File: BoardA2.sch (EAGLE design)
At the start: 4 parts, among them J1 CONN_12X2

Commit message: Update
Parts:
- removed J1: CONN_12X2, Smartcrutches:CONN_12X2
- added OSC: CLOCK-ECS-100X, Smartcrutches:CLOCK-ECS-100X
- C1: value (none) -> 0.1 uf
- IMU: value (none) -> AD7890-10
- U$1: value CLOCK-ECS-100X -> LOADCELLAMP; device Smartcrutches:CLOCK-ECS-100X -> Smartcrutches:LOADCELLAMP
- renumbered IC1 to IMU
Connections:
- new net CONVST: IMU.5
- new net DIN: IMU.11
- new net DOUT: IMU.10
- new net N$10: U$1.E+
- new net N$11: IMU.4
- new net N$12: U$1.E-
- new net N$13: U$1.A-
- new net N$14: U$1.A+
- new net N$15: U$1.SD
- new net N$7: U$1.DAT
- new net N$8: U$1.CLK
- new net RFS: IMU.9
- new net SCLK: IMU.7
- new net TFS: IMU.8
- new net UPPER1: IMU.16
- net 5V: now also OSC.+5V, U$1.VCC, U$1.VDD; no longer U$1.+5V
- net GND: now also C1.2, IMU.24, OSC.GND
- net N$2: now also IMU.17; no longer C1.2, IMU.24
- net N$4: now also OSC.OUT; no longer U$1.OUT

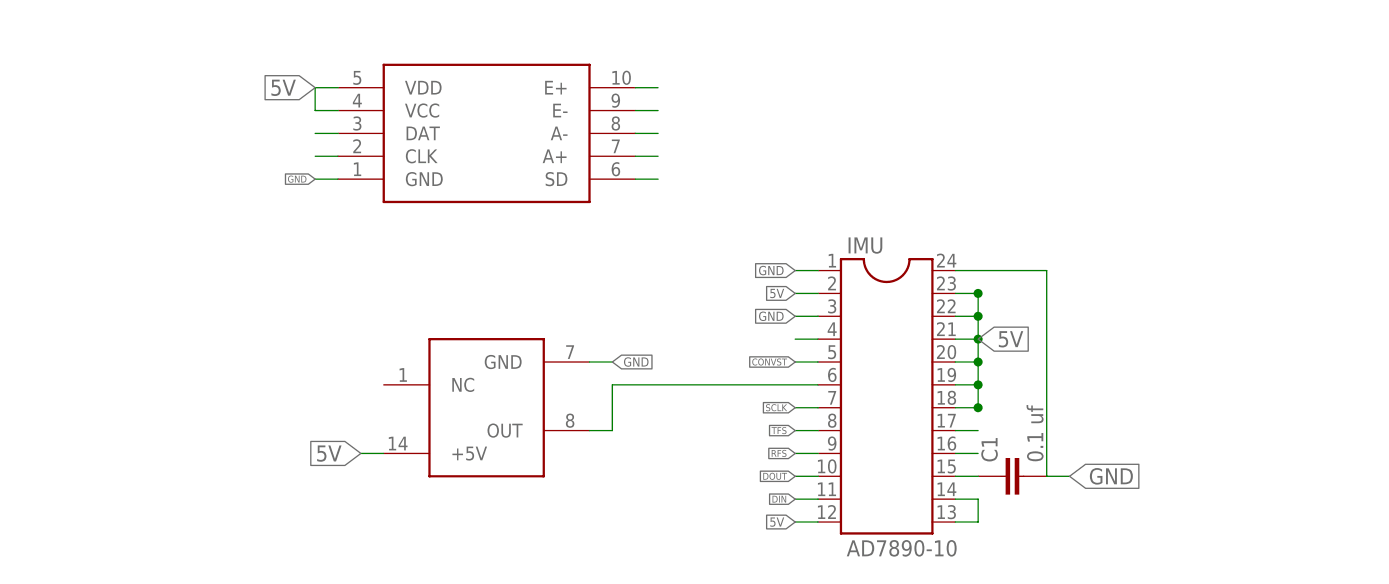
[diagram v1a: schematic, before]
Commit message: Updated both Boards
- Added holes
- Changed connectors
- routed both Boards
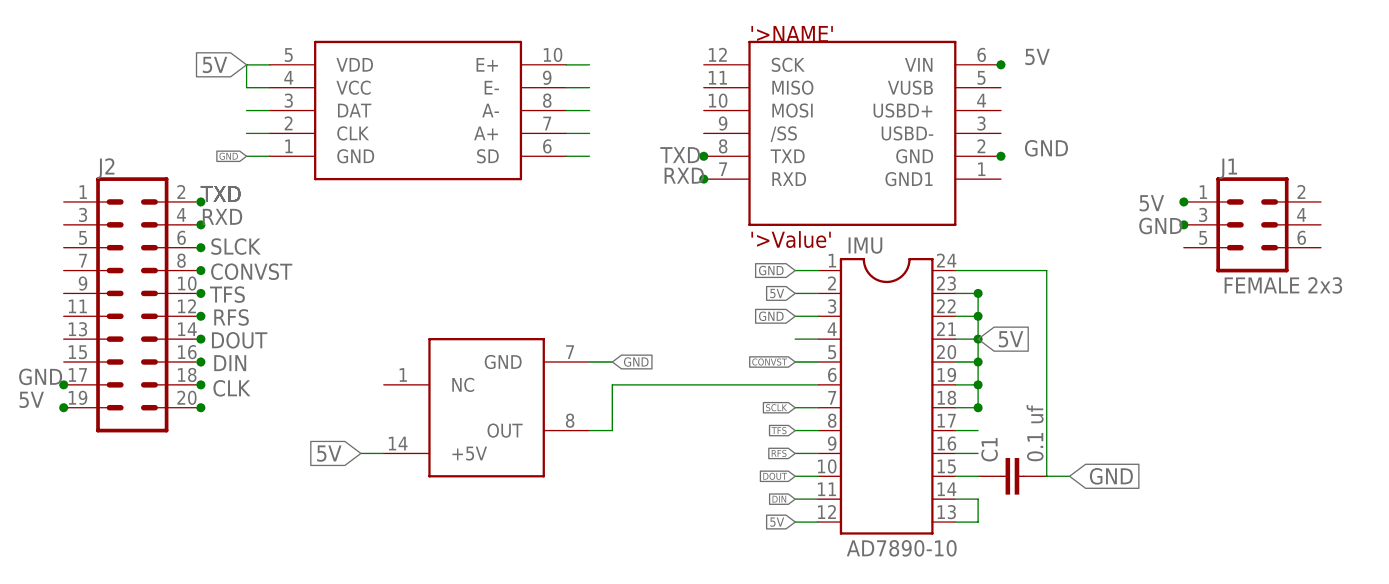
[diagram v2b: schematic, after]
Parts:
- added J1: FEMALE 2x3, SparkFun-Connectors:CONN_03X2FEMALE
- added J2: (no value), SparkFun-Connectors:CONN_10X2
- added U$2: IMU, Smartcrutches:IMU
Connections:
- new net CLK: J2.18
- new net N$22: J2.20
- new net RXD: J2.4, U$2.RXD
- new net SLCK: J2.6
- new net TXD: J2.2, U$2.TXD
- net 5V: now also IMU.2, J1.1, J2.19, U$2.VIN
- net CONVST: now also J2.8
- net DIN: now also J2.16
- net DOUT: now also J2.14
- net GND: now also IMU.1, J1.3, J2.17, U$2.GND
- net RFS: now also J2.12
- net TFS: now also J2.10
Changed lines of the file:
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@@
 <layer number="49" name="Reference" color="7" fill="1" visible="no" active="no"/>
 <layer number="50" name="dxf" color="7" fill="1" visible="no" active="no"/>
-<layer number="51" name="tDocu" color="9" fill="1" visible="no" active="no"/>
+<layer number="51" name="tDocu" color="7" fill="1" visible="no" active="no"/>
 <layer number="52" name="bDocu" color="7" fill="1" visible="no" active="no"/>
 <layer number="53" name="tGND_GNDA" color="7" fill="9" visible="no" active="no"/>
@@
 <part name="C1" library="SparkFun-Capacitors" deviceset="0.1UF-50V-20%(PTH)" device="KIT-EZ" value="0.1 uf"/>
 <part name="U$1" library="Smartcrutches" deviceset="LOADCELLAMP" device=""/>
+<part name="J1" library="SparkFun-Connectors" deviceset="CONN_03X2" device="FEMALE" value="FEMALE 2x3"/>
+<part name="U$2" library="Smartcrutches" deviceset="IMU" device=""/>
+<part name="J2" library="SparkFun-Connectors" deviceset="CONN_10X2" device=""/>
 </parts>
 <sheets>
@@
 <instance part="IMU" gate="G$1" x="-5.08" y="48.26"/>
 <instance part="C1" gate="G$1" x="10.16" y="40.64" rot="R90"/>
-<instance part="U$1" gate="G$1" x="-48.26" y="78.74"/>
+<instance part="U$1" gate="G$1" x="-55.88" y="81.28"/>
+<instance part="J1" gate="G$1" x="35.56" y="68.58"/>
+<instance part="U$2" gate="G$1" x="-10.16" y="78.74"/>
+<instance part="J2" gate="G$1" x="-88.9" y="60.96"/>
 </instances>
 <busses>
@@
 <segment>
 <wire x1="-12.7" y1="60.96" x2="-15.24" y2="60.96" width="0.1524" layer="91"/>
+<pinref part="IMU" gate="G$1" pin="2"/>
 </segment>
 <segment>
 <pinref part="U$1" gate="G$1" pin="VCC"/>
-<wire x1="-66.04" y1="81.28" x2="-68.58" y2="81.28" width="0.1524" layer="91"/>
+<wire x1="-73.66" y1="83.82" x2="-76.2" y2="83.82" width="0.1524" layer="91"/>
 <pinref part="U$1" gate="G$1" pin="VDD"/>
-<wire x1="-66.04" y1="83.82" x2="-68.58" y2="83.82" width="0.1524" layer="91"/>
-<wire x1="-68.58" y1="81.28" x2="-68.58" y2="83.82" width="0.1524" layer="91"/>
-<label x="-68.58" y="83.82" size="1.778" layer="95" rot="R180" xref="yes"/>
+<wire x1="-73.66" y1="86.36" x2="-76.2" y2="86.36" width="0.1524" layer="91"/>
+<wire x1="-76.2" y1="83.82" x2="-76.2" y2="86.36" width="0.1524" layer="91"/>
+<label x="-76.2" y="86.36" size="1.778" layer="95" rot="R180" xref="yes"/>
+</segment>
+<segment>
+<pinref part="J1" gate="G$1" pin="1"/>
+<junction x="27.94" y="71.12"/>
+<label x="22.86" y="70.104" size="1.778" layer="95"/>
+</segment>
+<segment>
+<pinref part="U$2" gate="G$1" pin="VIN"/>
+<junction x="7.62" y="86.36"/>
+<label x="10.16" y="86.36" size="1.778" layer="95"/>
+</segment>
+<segment>
+<pinref part="J2" gate="G$1" pin="19"/>
+<junction x="-96.52" y="48.26"/>
+<label x="-101.6" y="48.26" size="1.778" layer="95"/>
 </segment>
 </net>
@@
 <wire x1="-12.7" y1="63.5" x2="-15.24" y2="63.5" width="0.1524" layer="91"/>
 <label x="-15.24" y="63.5" size="1.016" layer="95" rot="R180" xref="yes"/>
+<pinref part="IMU" gate="G$1" pin="1"/>
 </segment>
 <segment>
@@
 <segment>
 <pinref part="U$1" gate="G$1" pin="GND"/>
-<wire x1="-66.04" y1="73.66" x2="-68.58" y2="73.66" width="0.1524" layer="91"/>
-<label x="-68.58" y="73.66" size="0.762" layer="95" rot="R180" xref="yes"/>
+<wire x1="-73.66" y1="76.2" x2="-76.2" y2="76.2" width="0.1524" layer="91"/>
+<label x="-76.2" y="76.2" size="0.762" layer="95" rot="R180" xref="yes"/>
+</segment>
+<segment>
+<pinref part="J1" gate="G$1" pin="3"/>
+<junction x="27.94" y="68.58"/>
+<label x="22.86" y="67.564" size="1.778" layer="95"/>
+</segment>
+<segment>
+<pinref part="U$2" gate="G$1" pin="GND"/>
+<junction x="7.62" y="76.2"/>
+<label x="10.16" y="76.2" size="1.778" layer="95"/>
+</segment>
+<segment>
+<pinref part="J2" gate="G$1" pin="17"/>
+<junction x="-96.52" y="50.8"/>
+<label x="-101.6" y="50.8" size="1.778" layer="95"/>
 </segment>
 </net>
@@
 <label x="-15.24" y="38.1" size="0.762" layer="95" rot="R180" xref="yes"/>
 </segment>
+<segment>
+<pinref part="J2" gate="G$1" pin="16"/>
+<junction x="-81.28" y="53.34"/>
+<label x="-80.01" y="52.324" size="1.778" layer="95"/>
+</segment>
 </net>
 <net name="DOUT" class="0">
@@
 <label x="-15.24" y="40.64" size="0.762" layer="95" rot="R180" xref="yes"/>
 </segment>
+<segment>
+<pinref part="J2" gate="G$1" pin="14"/>
+<junction x="-81.28" y="55.88"/>
+<label x="-80.264" y="54.864" size="1.778" layer="95"/>
+</segment>
 </net>
 <net name="RFS" class="0">
@@
 <label x="-15.24" y="43.18" size="0.762" layer="95" rot="R180" xref="yes"/>
 </segment>
+<segment>
+<pinref part="J2" gate="G$1" pin="12"/>
+<junction x="-81.28" y="58.42"/>
+<label x="-80.01" y="57.404" size="1.778" layer="95"/>
+</segment>
 </net>
 <net name="TFS" class="0">
@@
 <label x="-15.24" y="45.72" size="0.762" layer="95" rot="R180" xref="yes"/>
 </segment>
+<segment>
+<pinref part="J2" gate="G$1" pin="10"/>
+<junction x="-81.28" y="60.96"/>
+<label x="-80.264" y="59.944" size="1.778" layer="95"/>
+</segment>
 </net>
 <net name="SCLK" class="0">
@@
 <label x="-15.24" y="53.34" size="0.762" layer="95" rot="R180" xref="yes"/>
 </segment>
+<segment>
+<pinref part="J2" gate="G$1" pin="8"/>
+<junction x="-81.28" y="63.5"/>
+<label x="-80.264" y="62.484" size="1.778" layer="95"/>
+</segment>
 </net>
 <net name="N$11" class="0">
@@
 <segment>
 <pinref part="U$1" gate="G$1" pin="DAT"/>
-<wire x1="-66.04" y1="78.74" x2="-68.58" y2="78.74" width="0.1524" layer="91"/>
+<wire x1="-73.66" y1="81.28" x2="-76.2" y2="81.28" width="0.1524" layer="91"/>
 </segment>
 </net>
@@
 <segment>
 <pinref part="U$1" gate="G$1" pin="CLK"/>
-<wire x1="-66.04" y1="76.2" x2="-68.58" y2="76.2" width="0.1524" layer="91"/>
+<wire x1="-73.66" y1="78.74" x2="-76.2" y2="78.74" width="0.1524" layer="91"/>
 </segment>
 </net>
@@
 <segment>
 <pinref part="U$1" gate="G$1" pin="E+"/>
-<wire x1="-33.02" y1="83.82" x2="-30.48" y2="83.82" width="0.1524" layer="91"/>
+<wire x1="-40.64" y1="86.36" x2="-38.1" y2="86.36" width="0.1524" layer="91"/>
 </segment>
 </net>
@@
 <segment>
 <pinref part="U$1" gate="G$1" pin="E-"/>
-<wire x1="-33.02" y1="81.28" x2="-30.48" y2="81.28" width="0.1524" layer="91"/>
+<wire x1="-40.64" y1="83.82" x2="-38.1" y2="83.82" width="0.1524" layer="91"/>
 </segment>
 </net>
@@
 <segment>
 <pinref part="U$1" gate="G$1" pin="A-"/>
-<wire x1="-33.02" y1="78.74" x2="-30.48" y2="78.74" width="0.1524" layer="91"/>
+<wire x1="-40.64" y1="81.28" x2="-38.1" y2="81.28" width="0.1524" layer="91"/>
 </segment>
 </net>
@@
 <segment>
 <pinref part="U$1" gate="G$1" pin="A+"/>
-<wire x1="-33.02" y1="76.2" x2="-30.48" y2="76.2" width="0.1524" layer="91"/>
+<wire x1="-40.64" y1="78.74" x2="-38.1" y2="78.74" width="0.1524" layer="91"/>
 </segment>
 </net>
@@
 <segment>
 <pinref part="U$1" gate="G$1" pin="SD"/>
-<wire x1="-33.02" y1="73.66" x2="-30.48" y2="73.66" width="0.1524" layer="91"/>
-</segment>
-</net>
+<wire x1="-40.64" y1="76.2" x2="-38.1" y2="76.2" width="0.1524" layer="91"/>
+</segment>
+</net>
+<net name="TXD" class="0">
+<segment>
+<pinref part="J2" gate="G$1" pin="2"/>
+<junction x="-81.28" y="71.12"/>
+<label x="-81.28" y="71.12" size="1.778" layer="95"/>
+<label x="-81.28" y="71.12" size="1.778" layer="95"/>
+<label x="-81.28" y="71.12" size="1.778" layer="95"/>
+</segment>
+<segment>
+<pinref part="U$2" gate="G$1" pin="TXD"/>
+<junction x="-25.4" y="76.2"/>
+<label x="-30.226" y="75.438" size="1.778" layer="95"/>
+</segment>
+</net>
+<net name="RXD" class="0">
+<segment>
+<pinref part="J2" gate="G$1" pin="4"/>
+<junction x="-81.28" y="68.58"/>
+<label x="-81.28" y="68.58" size="1.778" layer="95"/>
+</segment>
+<segment>
+<pinref part="U$2" gate="G$1" pin="RXD"/>
+<junction x="-25.4" y="73.66"/>
+<label x="-29.972" y="73.152" size="1.778" layer="95"/>
+</segment>
+</net>
+<net name="SLCK" class="0">
+<segment>
+<pinref part="J2" gate="G$1" pin="6"/>
+<junction x="-81.28" y="66.04"/>
+<label x="-80.264" y="65.278" size="1.778" layer="95"/>
+</segment>
+</net>
+<net name="CLK" class="0">
+<segment>
+<pinref part="J2" gate="G$1" pin="18"/>
+<junction x="-81.28" y="50.8"/>
+<label x="-80.01" y="49.53" size="1.778" layer="95"/>
+</segment>
+</net>
+<net name="N$22" class="0">
+<segment>
+<pinref part="J2" gate="G$1" pin="20"/>
+<junction x="-81.28" y="48.26"/>
+</segment>
+</net>

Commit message: Routing Update
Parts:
- removed U$1: LOADCELLAMP, Smartcrutches:LOADCELLAMP
- removed U$2: IMU, Smartcrutches:IMU
- added ADC: AD7890-10, ic-package:DIL24-4
- added LOADCELL_AMP: HX711, Smartcrutches:LOADCELLAMP
- IMU: value AD7890-10 -> TSS-EM/3Space; device ic-package:DIL24-4 -> Smartcrutches:IMU
- renumbered OSC to OSCILLATOR
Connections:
- removed net N$10: U$1.E+
- removed net N$12: U$1.E-
- removed net N$13: U$1.A-
- removed net N$14: U$1.A+
- removed net N$15: U$1.SD
- removed net N$7: U$1.DAT
- removed net N$8: U$1.CLK
- net 5V: now also ADC.12, ADC.18, ADC.19, ADC.2, ADC.20, ADC.21, ADC.22, ADC.23, IMU.VIN, LOADCELL_AMP.VCC, LOADCELL_AMP.VDD; no longer IMU.12, IMU.18, IMU.19, IMU.2, IMU.20, IMU.21, IMU.22, IMU.23, U$1.VCC, U$1.VDD, U$2.VIN
- net CONVST: now also ADC.5; no longer IMU.5
- net DIN: now also ADC.11; no longer IMU.11
- net DOUT: now also ADC.10; no longer IMU.10
- net GND: now also ADC.1, ADC.24, ADC.3, IMU.GND, LOADCELL_AMP.GND; no longer IMU.1, IMU.24, IMU.3, U$1.GND, U$2.GND
- net N$1: now also ADC.13, ADC.14; no longer IMU.13, IMU.14
- net N$11: now also ADC.4; no longer IMU.4
- net N$2: now also ADC.17; no longer IMU.17
- net N$3: now also ADC.15; no longer IMU.15
- net N$4: now also ADC.6; no longer IMU.6
- net RFS: now also ADC.9; no longer IMU.9
- net RXD: now also IMU.RXD; no longer U$2.RXD
- net SCLK: now also ADC.7; no longer IMU.7
- net TFS: now also ADC.8; no longer IMU.8
- net TXD: now also IMU.TXD; no longer U$2.TXD
- net UPPER1: now also ADC.16; no longer IMU.16

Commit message: Routing and connection update
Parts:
- added J3: (no value), SparkFun-Connectors:CONN_04
- added J4: (no value), SparkFun-Connectors:CONN_01
- J2: device SparkFun-Connectors:CONN_10X2 -> SparkFun-Connectors:CONN_04
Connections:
- removed net CLK: J2.18
- removed net N$22: J2.20
- net 5V: no longer J2.19
- net CONVST: now also J4.1; no longer J2.8
- net DIN: now also J2.4; no longer J2.16
- net DOUT: now also J2.3; no longer J2.14
- net GND: no longer J2.17
- net RFS: now also J3.4; no longer J2.12
- net RXD: now also J2.2; no longer J2.4
- net SLCK: now also J3.1; no longer J2.6
- net TFS: now also J3.3; no longer J2.10
- net TXD: now also J2.1; no longer J2.2
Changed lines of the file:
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@@
 <part name="J1" library="SparkFun-Connectors" deviceset="CONN_03X2" device="FEMALE" value="FEMALE 2x3"/>
 <part name="IMU" library="Smartcrutches" deviceset="IMU" device="" value="TSS-EM/3Space"/>
-<part name="J2" library="SparkFun-Connectors" deviceset="CONN_10X2" device=""/>
 <part name="LOADCELL_AMP" library="Smartcrutches" deviceset="LOADCELLAMP" device="" value="HX711"/>
+<part name="J2" library="SparkFun-Connectors" deviceset="CONN_04" device=""/>
+<part name="J3" library="SparkFun-Connectors" deviceset="CONN_04" device=""/>
+<part name="J4" library="SparkFun-Connectors" deviceset="CONN_01" device=""/>
 </parts>
 <sheets>
@@
 <instance part="J1" gate="G$1" x="35.56" y="68.58"/>
 <instance part="IMU" gate="G$1" x="-7.62" y="83.82"/>
-<instance part="J2" gate="G$1" x="-88.9" y="60.96"/>
 <instance part="LOADCELL_AMP" gate="G$1" x="-55.88" y="86.36"/>
+<instance part="J2" gate="G$1" x="-35.56" y="68.58"/>
+<instance part="J3" gate="G$1" x="25.4" y="86.36"/>
+<instance part="J4" gate="G$1" x="-60.96" y="71.12"/>
 </instances>
 <busses>
@@
 </segment>
 <segment>
-<pinref part="J2" gate="G$1" pin="19"/>
-<junction x="-96.52" y="48.26"/>
-<label x="-101.6" y="48.26" size="1.778" layer="95"/>
-</segment>
-<segment>
 <pinref part="LOADCELL_AMP" gate="G$1" pin="VDD"/>
 <junction x="-73.66" y="91.44"/>
@@
 </segment>
 <segment>
-<pinref part="J2" gate="G$1" pin="17"/>
-<junction x="-96.52" y="50.8"/>
-<label x="-101.6" y="50.8" size="1.778" layer="95"/>
-</segment>
-<segment>
 <pinref part="LOADCELL_AMP" gate="G$1" pin="GND"/>
 <junction x="-73.66" y="81.28"/>
@@
 </segment>
 <segment>
-<pinref part="J2" gate="G$1" pin="16"/>
-<junction x="-81.28" y="53.34"/>
-<label x="-80.01" y="52.324" size="1.778" layer="95"/>
+<pinref part="J2" gate="G$1" pin="4"/>
+<junction x="-30.48" y="73.66"/>
+<label x="-29.718" y="72.898" size="1.778" layer="95"/>
 </segment>
 </net>
@@
 </segment>
 <segment>
-<pinref part="J2" gate="G$1" pin="14"/>
-<junction x="-81.28" y="55.88"/>
-<label x="-80.264" y="54.864" size="1.778" layer="95"/>
+<pinref part="J2" gate="G$1" pin="3"/>
+<junction x="-30.48" y="71.12"/>
+<label x="-29.972" y="70.358" size="1.778" layer="95"/>
 </segment>
 </net>
@@
 </segment>
 <segment>
-<pinref part="J2" gate="G$1" pin="12"/>
-<junction x="-81.28" y="58.42"/>
-<label x="-80.01" y="57.404" size="1.778" layer="95"/>
+<pinref part="J3" gate="G$1" pin="4"/>
+<junction x="30.48" y="91.44"/>
+<label x="30.988" y="90.678" size="1.778" layer="95"/>
 </segment>
 </net>
@@
 </segment>
 <segment>
-<pinref part="J2" gate="G$1" pin="10"/>
-<junction x="-81.28" y="60.96"/>
-<label x="-80.264" y="59.944" size="1.778" layer="95"/>
+<pinref part="J3" gate="G$1" pin="3"/>
+<junction x="30.48" y="88.9"/>
+<label x="31.242" y="87.884" size="1.778" layer="95"/>
 </segment>
 </net>
@@
 </segment>
 <segment>
-<pinref part="J2" gate="G$1" pin="8"/>
-<junction x="-81.28" y="63.5"/>
-<label x="-80.264" y="62.484" size="1.778" layer="95"/>
+<pinref part="J4" gate="G$1" pin="1"/>
+<junction x="-53.34" y="71.12"/>
+<label x="-52.324" y="70.358" size="1.778" layer="95"/>
 </segment>
 </net>
@@
 </net>
 <net name="TXD" class="0">
-<segment>
-<pinref part="J2" gate="G$1" pin="2"/>
-<junction x="-81.28" y="71.12"/>
-<label x="-81.28" y="71.12" size="1.778" layer="95"/>
-<label x="-81.28" y="71.12" size="1.778" layer="95"/>
-<label x="-81.28" y="71.12" size="1.778" layer="95"/>
-</segment>
 <segment>
 <pinref part="IMU" gate="G$1" pin="TXD"/>
@@
 <label x="-22.86" y="81.28" size="1.016" layer="95" rot="R180" xref="yes"/>
 </segment>
+<segment>
+<pinref part="J2" gate="G$1" pin="1"/>
+<junction x="-30.48" y="66.04"/>
+<label x="-29.972" y="65.278" size="1.778" layer="95"/>
+</segment>
 </net>
 <net name="RXD" class="0">
-<segment>
-<pinref part="J2" gate="G$1" pin="4"/>
-<junction x="-81.28" y="68.58"/>
-<label x="-81.28" y="68.58" size="1.778" layer="95"/>
-</segment>
 <segment>
 <pinref part="IMU" gate="G$1" pin="RXD"/>
@@
 <label x="-22.86" y="78.74" size="1.016" layer="95" rot="R180" xref="yes"/>
 </segment>
+<segment>
+<pinref part="J2" gate="G$1" pin="2"/>
+<junction x="-30.48" y="68.58"/>
+<label x="-29.972" y="67.818" size="1.778" layer="95"/>
+</segment>
 </net>
 <net name="SLCK" class="0">
 <segment>
-<pinref part="J2" gate="G$1" pin="6"/>
-<junction x="-81.28" y="66.04"/>
-<label x="-80.264" y="65.278" size="1.778" layer="95"/>
-</segment>
-</net>
-<net name="CLK" class="0">
-<segment>
-<pinref part="J2" gate="G$1" pin="18"/>
-<junction x="-81.28" y="50.8"/>
-<label x="-80.01" y="49.53" size="1.778" layer="95"/>
-</segment>
-</net>
-<net name="N$22" class="0">
-<segment>
-<pinref part="J2" gate="G$1" pin="20"/>
-<junction x="-81.28" y="48.26"/>
-</segment>
-</net>
+<pinref part="J3" gate="G$1" pin="1"/>
+<junction x="30.48" y="83.82"/>
+<label x="31.496" y="83.058" size="1.778" layer="95"/>
+</segment>
+</net>
